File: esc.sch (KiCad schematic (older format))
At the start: 73 parts, among them IC1 4N25, IC2 LM25101, IC3 LM25101, IC4 LM25101, IC5 ATMEGA8-AI, P1 CONN_01X03, P2 CONN_01X03, P3 CONN_01X02, P4 CONN_02X02, P5 CONN_01X01, P6 CONN_01X01, Q1 MOSFET_N, Q10 MOSFET_N, Q11 MOSFET_N, Q12 MOSFET_N, Q2 MOSFET_N, Q3 MOSFET_N, Q4 MOSFET_N, Q5 MOSFET_N, Q6 MOSFET_N, Q7 MOSFET_N, Q8 MOSFET_N, Q9 MOSFET_N, U1 MCP1804, U2 LM2940 10V, Y1 RESONATEUR

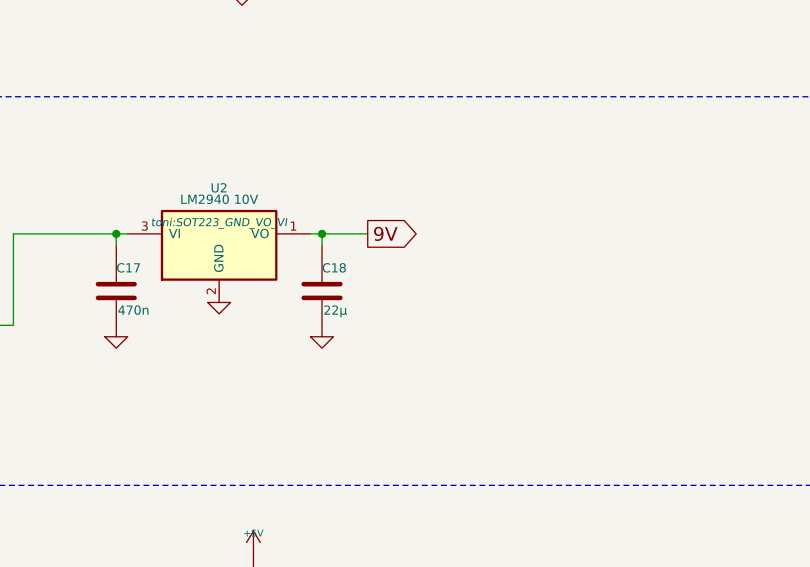
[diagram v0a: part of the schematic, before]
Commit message: Reduced part count, Splittet 22uF cap C17 into two 10uF
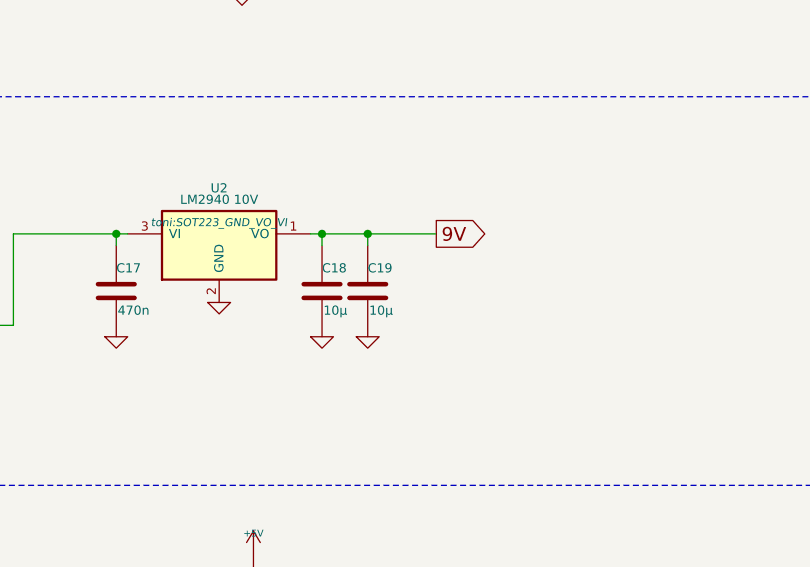
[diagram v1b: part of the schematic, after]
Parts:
- added C19: 10µ, Capacitors_SMD:C_1206, symbol C-RESCUE-esc
- C18: value 22µ -> 10µ
- C4, C5: footprint Capacitors_SMD:C_0805_HandSoldering -> Capacitors_SMD:C_1206
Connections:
- net 9V: now also C19.1
- net GND: now also C19.2
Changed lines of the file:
@@
 F 0 "C4" H 2550 4100 40  0000 L CNN
 F 1 "10µ" H 2556 3915 40  0000 L CNN
-F 2 "Capacitors_SMD:C_0805_HandSoldering" H 2588 3850 30  0001 C CNN
+F 2 "Capacitors_SMD:C_1206" H 2588 3850 30  0001 C CNN
 F 3 "" H 2550 4000 60  0000 C CNN
 	1    2550 4000
@@
 F 0 "C5" H 4000 4100 40  0000 L CNN
 F 1 "10µ" H 4006 3915 40  0000 L CNN
-F 2 "Capacitors_SMD:C_0805_HandSoldering" H 4038 3850 30  0001 C CNN
+F 2 "Capacitors_SMD:C_1206" H 4038 3850 30  0001 C CNN
 F 3 "" H 4000 4000 60  0000 C CNN
 	1    4000 4000
@@
 P 4000 6150
 F 0 "C18" H 4000 6250 40  0000 L CNN
-F 1 "22µ" H 4006 6065 40  0000 L CNN
+F 1 "10µ" H 4006 6065 40  0000 L CNN
 F 2 "Capacitors_SMD:C_1206" H 4038 6000 30  0001 C CNN
 F 3 "" H 4000 6150 60  0000 C CNN
@@
 	1    0    0    -1
 $EndComp
-Text GLabel 4200 5900 2    60   Output ~ 0
+Text GLabel 4500 5900 2    60   Output ~ 0
 9V
 Wire Wire Line
-	3950 5900 4200 5900
+	3950 5900 4500 5900
 Wire Wire Line
 	4000 5950 4000 5900
@@
 	0    -1   -1   0
 $EndComp
+$Comp
+L C-RESCUE-esc C19
+U 1 1 564EF8ED
+P 4200 6150
+F 0 "C19" H 4200 6250 40  0000 L CNN
+F 1 "10µ" H 4206 6065 40  0000 L CNN
+F 2 "Capacitors_SMD:C_1206" H 4238 6000 30  0001 C CNN
+F 3 "" H 4200 6150 60  0000 C CNN
+	1    4200 6150
+	1    0    0    -1
+$EndComp
+Wire Wire Line
+	4200 5900 4200 5950
+Connection ~ 4200 5900
+$Comp
+L GND-RESCUE-esc #PWR055
+U 1 1 564EFB64
+P 4200 6350
+F 0 "#PWR055" H 4200 6350 30  0001 C CNN
+F 1 "GND" H 4200 6280 30  0001 C CNN
+F 2 "" H 4200 6350 60  0000 C CNN
+F 3 "" H 4200 6350 60  0000 C CNN
+	1    4200 6350
+	1    0    0    -1
+$EndComp
 $EndSCHEMATC

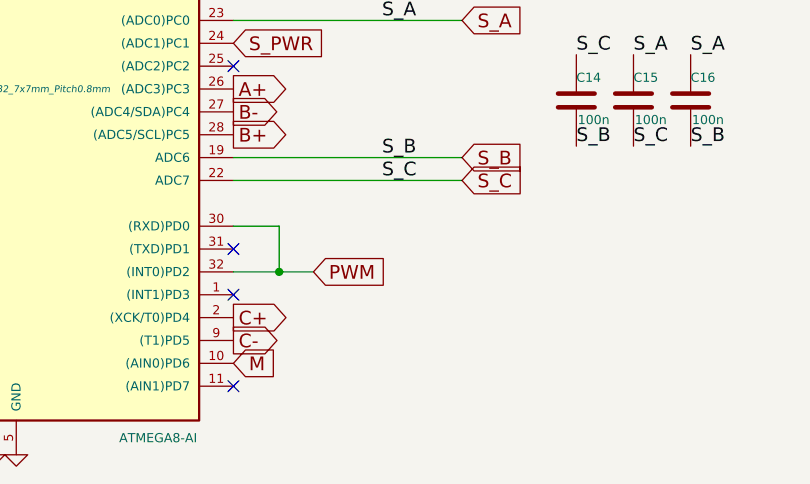
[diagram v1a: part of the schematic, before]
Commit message: PWR-on LED und Fault-LED eingefügt
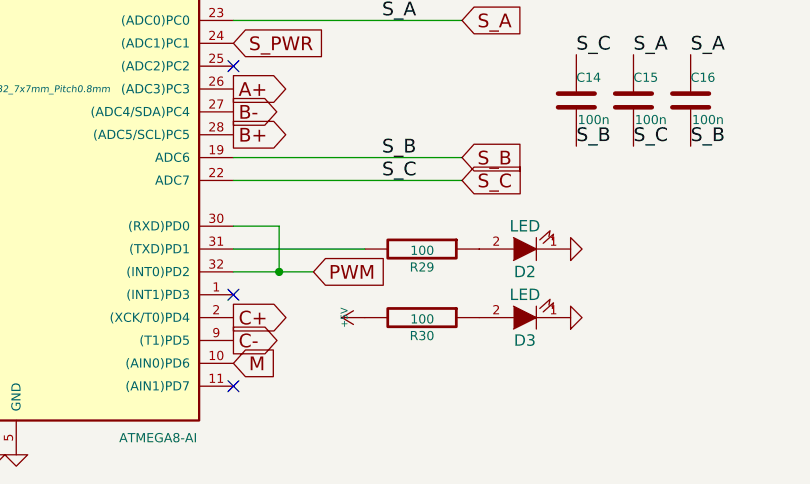
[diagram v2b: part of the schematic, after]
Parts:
- added D2, D3: LED, LEDs:LED-0805, symbol LED
- added R29, R30: 100, Resistors_SMD:R_0603_HandSoldering, symbol R-RESCUE-esc
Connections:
- net +5V: now also R30.2
- net GND: now also D2.1 (K), D3.1 (K)
- net at IC5.31 ((TXD)PD1): now also R29.2
- new net: D2.2 (A), R29.1
- new net: D3.2 (A), R30.1
- no-connect marks 10 -> 9
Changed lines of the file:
@@
 Text GLabel 4150 10000 2    60   Output ~ 0
 C+
-NoConn ~ 4150 9700
 NoConn ~ 4150 8100
 $Comp
@@
 	1    0    0    -1
 $EndComp
+$Comp
+L LED D2
+U 1 1 56535D91
+P 5425 9700
+F 0 "D2" H 5425 9800 50  0000 C CNN
+F 1 "LED" H 5425 9600 50  0000 C CNN
+F 2 "LEDs:LED-0805" H 5425 9700 60  0001 C CNN
+F 3 "" H 5425 9700 60  0000 C CNN
+	1    5425 9700
+	-1   0    0    1
+$EndComp
+$Comp
+L R-RESCUE-esc R29
+U 1 1 5653622E
+P 4975 9700
+F 0 "R29" V 5055 9700 40  0000 C CNN
+F 1 "100" V 4982 9701 40  0000 C CNN
+F 2 "Resistors_SMD:R_0603_HandSoldering" V 4905 9700 30  0001 C CNN
+F 3 "" H 4975 9700 30  0000 C CNN
+	1    4975 9700
+	0    1    1    0
+$EndComp
+Wire Wire Line
+	4725 9700 4150 9700
+$Comp
+L GND-RESCUE-esc #PWR056
+U 1 1 56536666
+P 5625 9700
+F 0 "#PWR056" H 5625 9700 30  0001 C CNN
+F 1 "GND" H 5625 9630 30  0001 C CNN
+F 2 "" H 5625 9700 60  0000 C CNN
+F 3 "" H 5625 9700 60  0000 C CNN
+	1    5625 9700
+	0    -1   -1   0
+$EndComp
+$Comp
+L LED D3
+U 1 1 56537251
+P 5425 10000
+F 0 "D3" H 5425 10100 50  0000 C CNN
+F 1 "LED" H 5425 9900 50  0000 C CNN
+F 2 "LEDs:LED-0805" H 5425 10000 60  0001 C CNN
+F 3 "" H 5425 10000 60  0000 C CNN
+	1    5425 10000
+	-1   0    0    1
+$EndComp
+$Comp
+L R-RESCUE-esc R30
+U 1 1 56537368
+P 4975 10000
+F 0 "R30" V 5055 10000 40  0000 C CNN
+F 1 "100" V 4982 10001 40  0000 C CNN
+F 2 "Resistors_SMD:R_0603_HandSoldering" V 4905 10000 30  0001 C CNN
+F 3 "" H 4975 10000 30  0000 C CNN
+	1    4975 10000
+	0    1    1    0
+$EndComp
+$Comp
+L GND-RESCUE-esc #PWR057
+U 1 1 5653747A
+P 5625 10000
+F 0 "#PWR057" H 5625 10000 30  0001 C CNN
+F 1 "GND" H 5625 9930 30  0001 C CNN
+F 2 "" H 5625 10000 60  0000 C CNN
+F 3 "" H 5625 10000 60  0000 C CNN
+	1    5625 10000
+	0    -1   -1   0
+$EndComp
+$Comp
+L +5V #PWR058
+U 1 1 56538633
+P 4725 10000
+F 0 "#PWR058" H 4725 10090 20  0001 C CNN
+F 1 "+5V" H 4725 10090 30  0000 C CNN
+F 2 "" H 4725 10000 60  0000 C CNN
+F 3 "" H 4725 10000 60  0000 C CNN
+	1    4725 10000
+	0    -1   -1   0
+$EndComp
 $EndSCHEMATC

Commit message: FET-Pins sind jetzt auf Solid umgestellt
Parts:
- C10, C12, C7: footprint Capacitors_SMD:C_0805_HandSoldering -> Capacitors_SMD:C_0603
- C14, C15, C16: footprint Capacitors_SMD:C_0603_HandSoldering -> Capacitors_SMD:C_0603
- C17: footprint Capacitors_SMD:C_0805_HandSoldering -> Capacitors_SMD:C_0805
- R10, R11, R12, R13, R14, R15, R16, R18, R19, R20, R21, R22, R23, R24, R25, R26, R27, R28, R29, R3, R30, R4, R5, R7, R8, R9: footprint Resistors_SMD:R_0603_HandSoldering -> Resistors_SMD:R_0603
- R2, R6: footprint Resistors_SMD:R_0805_HandSoldering -> Resistors_SMD:R_0603
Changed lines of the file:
@@
 F 0 "C10" H 3700 7600 40  0000 L CNN
 F 1 "100n" H 3706 7415 40  0000 L CNN
-F 2 "Capacitors_SMD:C_0805_HandSoldering" H 3738 7350 30  0001 C CNN
+F 2 "Capacitors_SMD:C_0603" H 3738 7350 30  0001 C CNN
 F 3 "" H 3700 7500 60  0000 C CNN
 	1    3700 7500
@@
 F 0 "C14" H 5650 9150 40  0000 L CNN
 F 1 "100n" H 5656 8965 40  0000 L CNN
-F 2 "Capacitors_SMD:C_0603_HandSoldering" H 5688 8900 30  0001 C CNN
+F 2 "Capacitors_SMD:C_0603" H 5688 8900 30  0001 C CNN
 F 3 "" H 5650 9050 60  0000 C CNN
 	1    5650 9050
@@
 F 0 "C15" H 5900 9150 40  0000 L CNN
 F 1 "100n" H 5906 8965 40  0000 L CNN
-F 2 "Capacitors_SMD:C_0603_HandSoldering" H 5938 8900 30  0001 C CNN
+F 2 "Capacitors_SMD:C_0603" H 5938 8900 30  0001 C CNN
 F 3 "" H 5900 9050 60  0000 C CNN
 	1    5900 9050
@@
 F 0 "C16" H 6150 9150 40  0000 L CNN
 F 1 "100n" H 6156 8965 40  0000 L CNN
-F 2 "Capacitors_SMD:C_0603_HandSoldering" H 6188 8900 30  0001 C CNN
+F 2 "Capacitors_SMD:C_0603" H 6188 8900 30  0001 C CNN
 F 3 "" H 6150 9050 60  0000 C CNN
 	1    6150 9050
@@
 F 0 "R6" V 2280 3750 40  0000 C CNN
 F 1 "1" V 2207 3751 40  0000 C CNN
-F 2 "Resistors_SMD:R_0805_HandSoldering" V 2130 3750 30  0001 C CNN
+F 2 "Resistors_SMD:R_0603" V 2130 3750 30  0001 C CNN
 F 3 "" H 2200 3750 30  0000 C CNN
 	1    2200 3750
@@
 F 0 "R7" V 3730 4100 40  0000 C CNN
 F 1 "1k5" V 3657 4101 40  0000 C CNN
-F 2 "Resistors_SMD:R_0603_HandSoldering" V 3580 4100 30  0001 C CNN
+F 2 "Resistors_SMD:R_0603" V 3580 4100 30  0001 C CNN
 F 3 "" H 3650 4100 30  0000 C CNN
 	1    3650 4100
@@
 F 0 "C7" H 3650 4750 40  0000 L CNN
 F 1 "100n" H 3656 4565 40  0000 L CNN
-F 2 "Capacitors_SMD:C_0805_HandSoldering" H 3688 4500 30  0001 C CNN
+F 2 "Capacitors_SMD:C_0603" H 3688 4500 30  0001 C CNN
 F 3 "" H 3650 4650 60  0000 C CNN
 	1    3650 4650
@@
 F 0 "R2" V 3030 1550 40  0000 C CNN
 F 1 "10k" V 2957 1551 40  0000 C CNN
-F 2 "Resistors_SMD:R_0805_HandSoldering" V 2880 1550 30  0001 C CNN
+F 2 "Resistors_SMD:R_0603" V 2880 1550 30  0001 C CNN
 F 3 "" H 2950 1550 30  0000 C CNN
 	1    2950 1550
@@
 F 0 "C12" H 2050 8400 40  0000 L CNN
 F 1 "100n" H 2056 8215 40  0000 L CNN
-F 2 "Capacitors_SMD:C_0805_HandSoldering" H 2088 8150 30  0001 C CNN
+F 2 "Capacitors_SMD:C_0603" H 2088 8150 30  0001 C CNN
 F 3 "" H 2050 8300 60  0000 C CNN
 	1    2050 8300
@@
 F 0 "R12" V 1530 8200 40  0000 C CNN
 F 1 "100" V 1457 8201 40  0000 C CNN
-F 2 "Resistors_SMD:R_0603_HandSoldering" V 1380 8200 30  0001 C CNN
+F 2 "Resistors_SMD:R_0603" V 1380 8200 30  0001 C CNN
 F 3 "" H 1450 8200 30  0000 C CNN
 	1    1450 8200
@@
 F 0 "R4" V 10780 2700 40  0000 C CNN
 F 1 "18k" V 10707 2701 40  0000 C CNN
-F 2 "Resistors_SMD:R_0603_HandSoldering" V 10630 2700 30  0001 C CNN
+F 2 "Resistors_SMD:R_0603" V 10630 2700 30  0001 C CNN
 F 3 "" H 10700 2700 30  0000 C CNN
 	1    10700 2700
@@
 F 0 "R5" V 10430 3250 40  0000 C CNN
 F 1 "3k3" V 10357 3251 40  0000 C CNN
-F 2 "Resistors_SMD:R_0603_HandSoldering" V 10280 3250 30  0001 C CNN
+F 2 "Resistors_SMD:R_0603" V 10280 3250 30  0001 C CNN
 F 3 "" H 10350 3250 30  0000 C CNN
 	1    10350 3250
@@
 F 0 "R3" V 10080 2700 40  0000 C CNN
 F 1 "3k3" V 10007 2701 40  0000 C CNN
-F 2 "Resistors_SMD:R_0603_HandSoldering" V 9930 2700 30  0001 C CNN
+F 2 "Resistors_SMD:R_0603" V 9930 2700 30  0001 C CNN
 F 3 "" H 10000 2700 30  0000 C CNN
 	1    10000 2700
@@
 F 0 "R9" V 10780 5350 40  0000 C CNN
 F 1 "18k" V 10707 5351 40  0000 C CNN
-F 2 "Resistors_SMD:R_0603_HandSoldering" V 10630 5350 30  0001 C CNN
+F 2 "Resistors_SMD:R_0603" V 10630 5350 30  0001 C CNN
 F 3 "" H 10700 5350 30  0000 C CNN
 	1    10700 5350
@@
 F 0 "R11" V 10430 5900 40  0000 C CNN
 F 1 "3k3" V 10357 5901 40  0000 C CNN
-F 2 "Resistors_SMD:R_0603_HandSoldering" V 10280 5900 30  0001 C CNN
+F 2 "Resistors_SMD:R_0603" V 10280 5900 30  0001 C CNN
 F 3 "" H 10350 5900 30  0000 C CNN
 	1    10350 5900
@@
 F 0 "R8" V 10080 5350 40  0000 C CNN
 F 1 "3k3" V 10007 5351 40  0000 C CNN
-F 2 "Resistors_SMD:R_0603_HandSoldering" V 9930 5350 30  0001 C CNN
+F 2 "Resistors_SMD:R_0603" V 9930 5350 30  0001 C CNN
 F 3 "" H 10000 5350 30  0000 C CNN
 	1    10000 5350
@@
 F 0 "R14" V 10780 8250 40  0000 C CNN
 F 1 "18k" V 10707 8251 40  0000 C CNN
-F 2 "Resistors_SMD:R_0603_HandSoldering" V 10630 8250 30  0001 C CNN
+F 2 "Resistors_SMD:R_0603" V 10630 8250 30  0001 C CNN
 F 3 "" H 10700 8250 30  0000 C CNN
 	1    10700 8250
@@
 F 0 "R15" V 10430 8800 40  0000 C CNN
 F 1 "3k3" V 10357 8801 40  0000 C CNN
-F 2 "Resistors_SMD:R_0603_HandSoldering" V 10280 8800 30  0001 C CNN
+F 2 "Resistors_SMD:R_0603" V 10280 8800 30  0001 C CNN
 F 3 "" H 10350 8800 30  0000 C CNN
 	1    10350 8800
@@
 F 0 "R13" V 10080 8250 40  0000 C CNN
 F 1 "3k3" V 10007 8251 40  0000 C CNN
-F 2 "Resistors_SMD:R_0603_HandSoldering" V 9930 8250 30  0001 C CNN
+F 2 "Resistors_SMD:R_0603" V 9930 8250 30  0001 C CNN
 F 3 "" H 10000 8250 30  0000 C CNN
 	1    10000 8250
@@
 F 0 "R16" V 2330 7750 40  0000 C CNN
 F 1 "3k3" V 2257 7751 40  0000 C CNN
-F 2 "Resistors_SMD:R_0603_HandSoldering" V 2180 7750 30  0001 C CNN
+F 2 "Resistors_SMD:R_0603" V 2180 7750 30  0001 C CNN
 F 3 "" H 2250 7750 30  0000 C CNN
 	1    2250 7750
@@
 F 0 "C17" H 3100 6250 40  0000 L CNN
 F 1 "470n" H 3106 6065 40  0000 L CNN
-F 2 "Capacitors_SMD:C_0805_HandSoldering" H 3138 6000 30  0001 C CNN
+F 2 "Capacitors_SMD:C_0805" H 3138 6000 30  0001 C CNN
 F 3 "" H 3100 6150 60  0000 C CNN
 	1    3100 6150
@@
 F 0 "R21" V 13030 8050 40  0000 C CNN
 F 1 "R" V 12957 8051 40  0000 C CNN
-F 2 "Resistors_SMD:R_0603_HandSoldering" V 12880 8050 30  0001 C CNN
+F 2 "Resistors_SMD:R_0603" V 12880 8050 30  0001 C CNN
 F 3 "" H 12950 8050 30  0000 C CNN
 	1    12950 8050
@@
 F 0 "R22" V 13030 8550 40  0000 C CNN
 F 1 "R" V 12957 8551 40  0000 C CNN
-F 2 "Resistors_SMD:R_0603_HandSoldering" V 12880 8550 30  0001 C CNN
+F 2 "Resistors_SMD:R_0603" V 12880 8550 30  0001 C CNN
 F 3 "" H 12950 8550 30  0000 C CNN
 	1    12950 8550
@@
 F 0 "R20" V 13030 5650 40  0000 C CNN
 F 1 "R" V 12957 5651 40  0000 C CNN
-F 2 "Resistors_SMD:R_0603_HandSoldering" V 12880 5650 30  0001 C CNN
+F 2 "Resistors_SMD:R_0603" V 12880 5650 30  0001 C CNN
 F 3 "" H 12950 5650 30  0000 C CNN
 	1    12950 5650
@@
 F 0 "R19" V 13030 5150 40  0000 C CNN
 F 1 "R" V 12957 5151 40  0000 C CNN
-F 2 "Resistors_SMD:R_0603_HandSoldering" V 12880 5150 30  0001 C CNN
+F 2 "Resistors_SMD:R_0603" V 12880 5150 30  0001 C CNN
 F 3 "" H 12950 5150 30  0000 C CNN
 	1    12950 5150
@@
 F 0 "R18" V 13030 3000 40  0000 C CNN
 F 1 "R" V 12957 3001 40  0000 C CNN
-F 2 "Resistors_SMD:R_0603_HandSoldering" V 12880 3000 30  0001 C CNN
+F 2 "Resistors_SMD:R_0603" V 12880 3000 30  0001 C CNN
 F 3 "" H 12950 3000 30  0000 C CNN
 	1    12950 3000
@@
 F 0 "R10" V 13030 2500 40  0000 C CNN
 F 1 "R" V 12957 2501 40  0000 C CNN
-F 2 "Resistors_SMD:R_0603_HandSoldering" V 12880 2500 30  0001 C CNN
+F 2 "Resistors_SMD:R_0603" V 12880 2500 30  0001 C CNN
 F 3 "" H 12950 2500 30  0000 C CNN
 	1    12950 2500
@@
 F 0 "R27" V 10130 7350 50  0000 C CNN
 F 1 "PD" V 10050 7350 50  0000 C CNN
-F 2 "Resistors_SMD:R_0603_HandSoldering" V 9980 7350 30  0001 C CNN
+F 2 "Resistors_SMD:R_0603" V 9980 7350 30  0001 C CNN
 F 3 "" H 10050 7350 30  0000 C CNN
 	1    10050 7350
@@
 F 0 "R28" V 10130 7500 50  0000 C CNN
 F 1 "PD" V 10050 7500 50  0000 C CNN
-F 2 "Resistors_SMD:R_0603_HandSoldering" V 9980 7500 30  0001 C CNN
+F 2 "Resistors_SMD:R_0603" V 9980 7500 30  0001 C CNN
 F 3 "" H 10050 7500 30  0000 C CNN
 	1    10050 7500
@@
 F 0 "R25" V 10180 4600 50  0000 C CNN
 F 1 "PD" V 10100 4600 50  0000 C CNN
-F 2 "Resistors_SMD:R_0603_HandSoldering" V 10030 4600 30  0001 C CNN
+F 2 "Resistors_SMD:R_0603" V 10030 4600 30  0001 C CNN
 F 3 "" H 10100 4600 30  0000 C CNN
 	1    10100 4600
@@
 F 0 "R26" V 10180 4750 50  0000 C CNN
 F 1 "PD" V 10100 4750 50  0000 C CNN
-F 2 "Resistors_SMD:R_0603_HandSoldering" V 10030 4750 30  0001 C CNN
+F 2 "Resistors_SMD:R_0603" V 10030 4750 30  0001 C CNN
 F 3 "" H 10100 4750 30  0000 C CNN
 	1    10100 4750
@@
 F 0 "R23" V 10180 1900 50  0000 C CNN
 F 1 "PD" V 10100 1900 50  0000 C CNN
-F 2 "Resistors_SMD:R_0603_HandSoldering" V 10030 1900 30  0001 C CNN
+F 2 "Resistors_SMD:R_0603" V 10030 1900 30  0001 C CNN
 F 3 "" H 10100 1900 30  0000 C CNN
 	1    10100 1900
@@
 F 0 "R24" V 10180 2100 50  0000 C CNN
 F 1 "PD" V 10100 2100 50  0000 C CNN
-F 2 "Resistors_SMD:R_0603_HandSoldering" V 10030 2100 30  0001 C CNN
+F 2 "Resistors_SMD:R_0603" V 10030 2100 30  0001 C CNN
 F 3 "" H 10100 2100 30  0000 C CNN
 	1    10100 2100
@@
 F 0 "R29" V 5055 9700 40  0000 C CNN
 F 1 "100" V 4982 9701 40  0000 C CNN
-F 2 "Resistors_SMD:R_0603_HandSoldering" V 4905 9700 30  0001 C CNN
+F 2 "Resistors_SMD:R_0603" V 4905 9700 30  0001 C CNN
 F 3 "" H 4975 9700 30  0000 C CNN
 	1    4975 9700
@@
 F 0 "R30" V 5055 10000 40  0000 C CNN
 F 1 "100" V 4982 10001 40  0000 C CNN
-F 2 "Resistors_SMD:R_0603_HandSoldering" V 4905 10000 30  0001 C CNN
+F 2 "Resistors_SMD:R_0603" V 4905 10000 30  0001 C CNN
 F 3 "" H 4975 10000 30  0000 C CNN
 	1    4975 10000

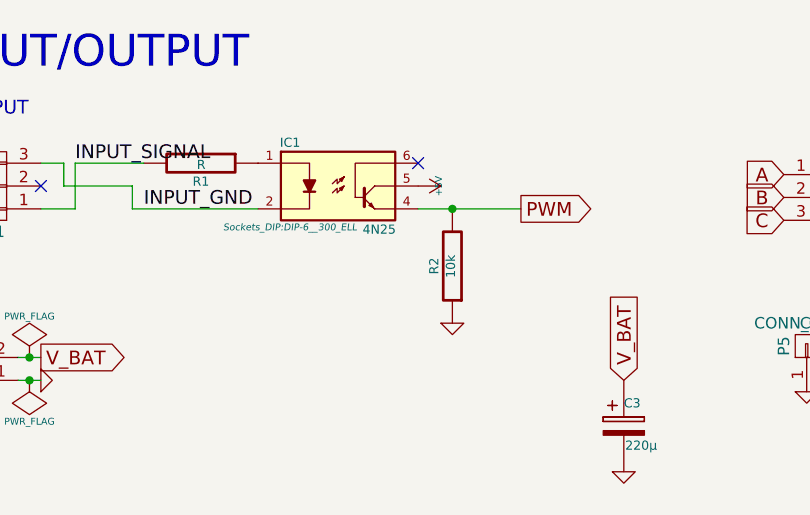
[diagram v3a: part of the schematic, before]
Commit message: Optokoppler zu LTV-356T weil muss so
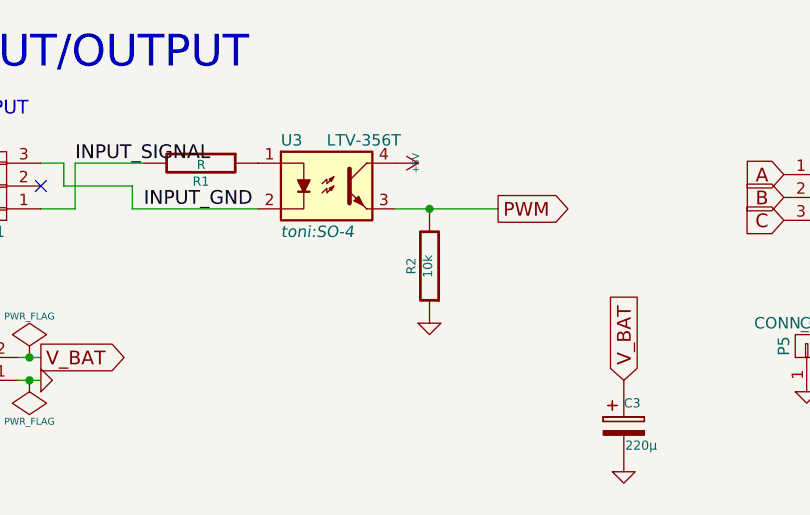
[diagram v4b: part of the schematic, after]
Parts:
- removed IC1: 4N25, Sockets_DIP:DIP-6__300_ELL, symbol 4N25-RESCUE-esc
- added U3: LTV-356T, toni:SO-4, symbol LTV-817
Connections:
- net +5V: now also U3.4
- net INPUT_GND: now also U3.2
- net PWM: now also U3.3
- net at R1.1: now also U3.1
- no-connect marks 9 -> 8
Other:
- moved on the sheet: R2
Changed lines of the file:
@@
 BAT
-$Comp
-L 4N25-RESCUE-esc IC1
-U 1 1 564459C3
-P 2450 1200
-F 0 "IC1" H 2240 1390 40  0000 C CNN
-F 1 "4N25" H 2630 1010 40  0000 C CNN
-F 2 "Sockets_DIP:DIP-6__300_ELL" H 2240 1020 30  0000 C CIN
-F 3 "" H 2450 1200 60  0000 C CNN
-	1    2450 1200
-	1    0    0    -1
-$EndComp
 $Comp
 L R-RESCUE-esc R1
@@
 Text Label 1600 1300 0    60   ~ 0
 INPUT_GND
-Text GLabel 3250 1300 2    60   Output ~ 0
+Text GLabel 3150 1300 2    60   Output ~ 0
 PWM
 Wire Wire Line
@@
 $EndComp
 NoConn ~ 4150 9900
-NoConn ~ 2800 1100
 $Comp
 L +5V #PWR017
 U 1 1 5644964D
-P 2800 1200
-F 0 "#PWR017" H 2800 1290 20  0001 C CNN
-F 1 "+5V" H 2800 1290 30  0000 C CNN
-F 2 "" H 2800 1200 60  0000 C CNN
-F 3 "" H 2800 1200 60  0000 C CNN
-	1    2800 1200
-	0    1    1    0
-$EndComp
-Connection ~ 2950 1300
-Wire Wire Line
-	2800 1300 3250 1300
+P 2700 1100
+F 0 "#PWR017" H 2700 1190 20  0001 C CNN
+F 1 "+5V" H 2700 1190 30  0000 C CNN
+F 2 "" H 2700 1100 60  0000 C CNN
+F 3 "" H 2700 1100 60  0000 C CNN
+	1    2700 1100
+	0    1    1    0
+$EndComp
+Connection ~ 2850 1300
+Wire Wire Line
+	2700 1300 3150 1300
 $Comp
 L R-RESCUE-esc R2
 U 1 1 56449896
-P 2950 1550
-F 0 "R2" V 3030 1550 40  0000 C CNN
-F 1 "10k" V 2957 1551 40  0000 C CNN
-F 2 "Resistors_SMD:R_0603" V 2880 1550 30  0001 C CNN
-F 3 "" H 2950 1550 30  0000 C CNN
-	1    2950 1550
+P 2850 1550
+F 0 "R2" V 2930 1550 40  0000 C CNN
+F 1 "10k" V 2857 1551 40  0000 C CNN
+F 2 "Resistors_SMD:R_0603" V 2780 1550 30  0001 C CNN
+F 3 "" H 2850 1550 30  0000 C CNN
+	1    2850 1550
 	-1   0    0    1
 $EndComp
@@
 L GND-RESCUE-esc #PWR018
 U 1 1 5644A8F1
-P 2950 1800
-F 0 "#PWR018" H 2950 1800 30  0001 C CNN
-F 1 "GND" H 2950 1730 30  0001 C CNN
-F 2 "" H 2950 1800 60  0000 C CNN
-F 3 "" H 2950 1800 60  0000 C CNN
-	1    2950 1800
+P 2850 1800
+F 0 "#PWR018" H 2850 1800 30  0001 C CNN
+F 1 "GND" H 2850 1730 30  0001 C CNN
+F 2 "" H 2850 1800 60  0000 C CNN
+F 3 "" H 2850 1800 60  0000 C CNN
+	1    2850 1800
 	1    0    0    -1
 $EndComp
@@
 	0    -1   -1   0
 $EndComp
+$Comp
+L LTV-817 U3
+U 1 1 56545590
+P 2400 1200
+F 0 "U3" H 2200 1400 50  0000 L CNN
+F 1 "LTV-356T" H 2400 1400 50  0000 L CNN
+F 2 "toni:SO-4" H 2200 1000 50  0000 L CIN
+F 3 "" H 2400 1100 50  0000 L CNN
+	1    2400 1200
+	1    0    0    -1
+$EndComp
 $EndSCHEMATC
